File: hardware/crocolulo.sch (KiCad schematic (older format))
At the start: 8 parts, among them P1 CONN_02X14, P2 CONN_01X04, U1 stk682

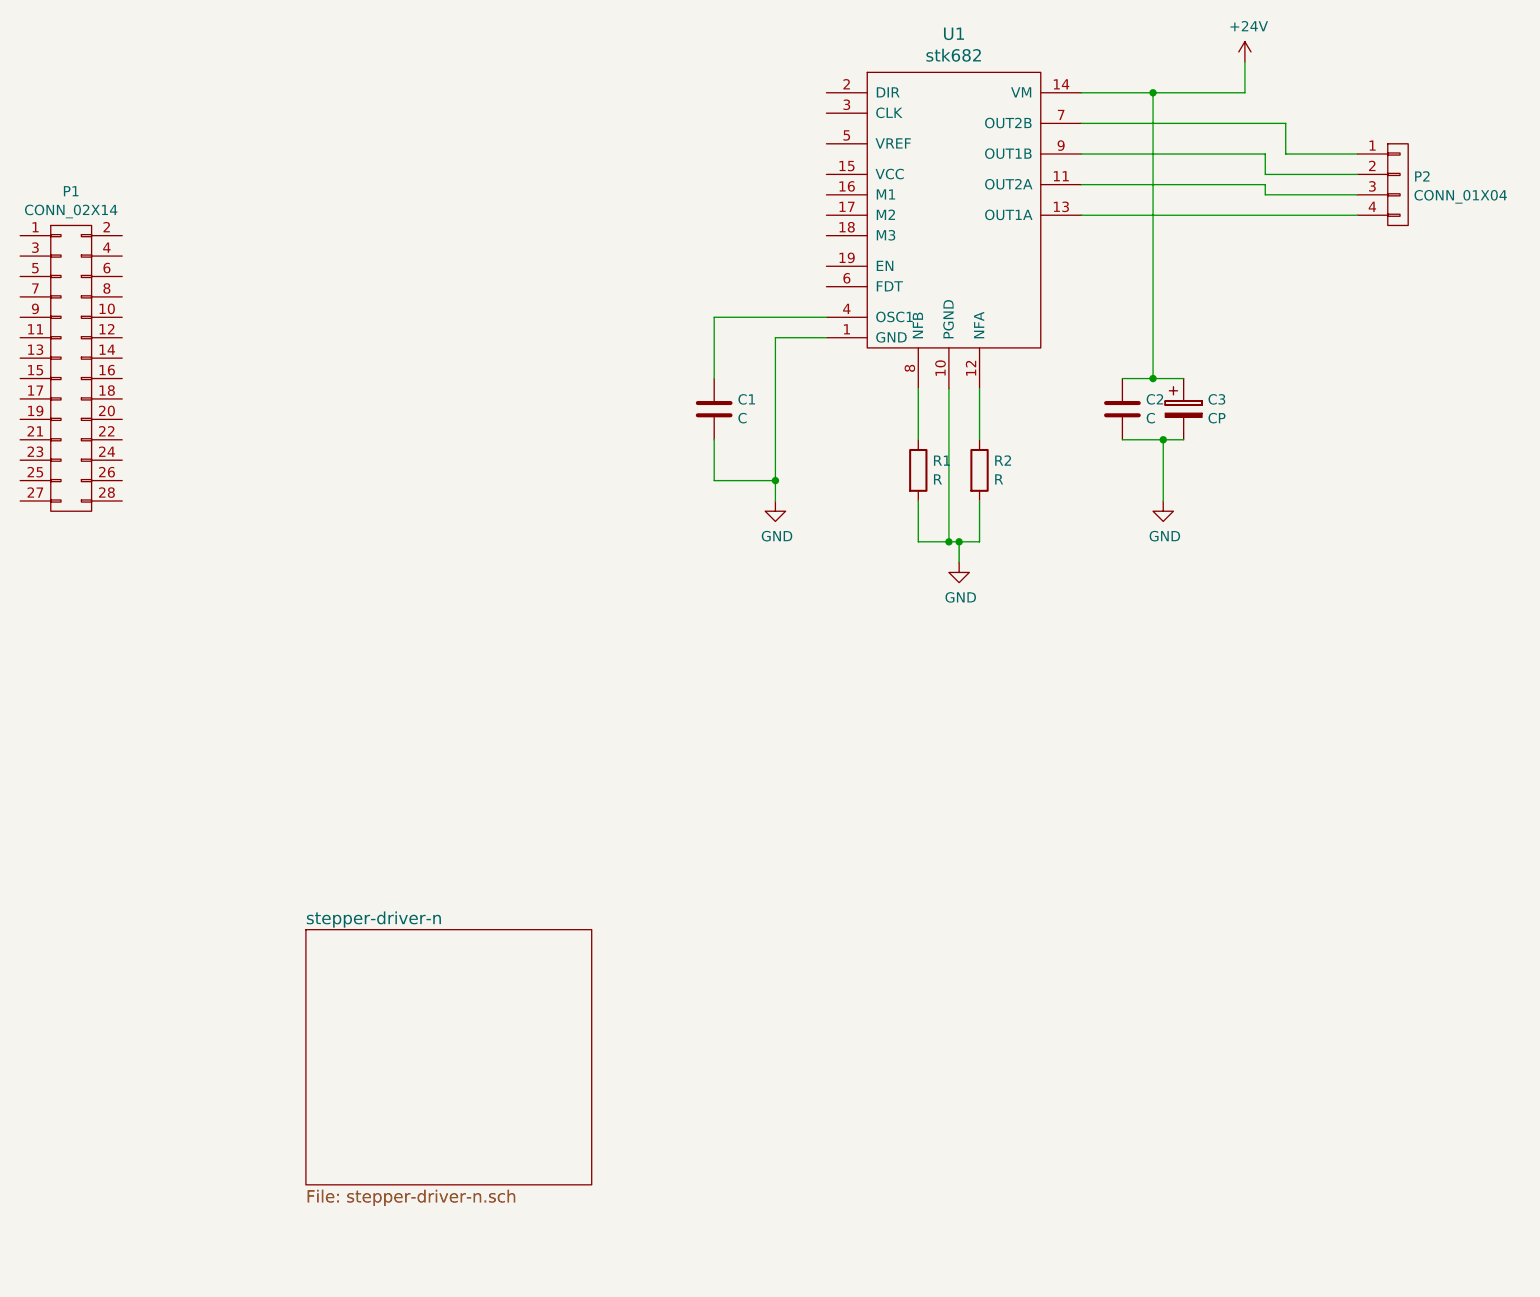
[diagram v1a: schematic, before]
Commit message: Add more sub sheets
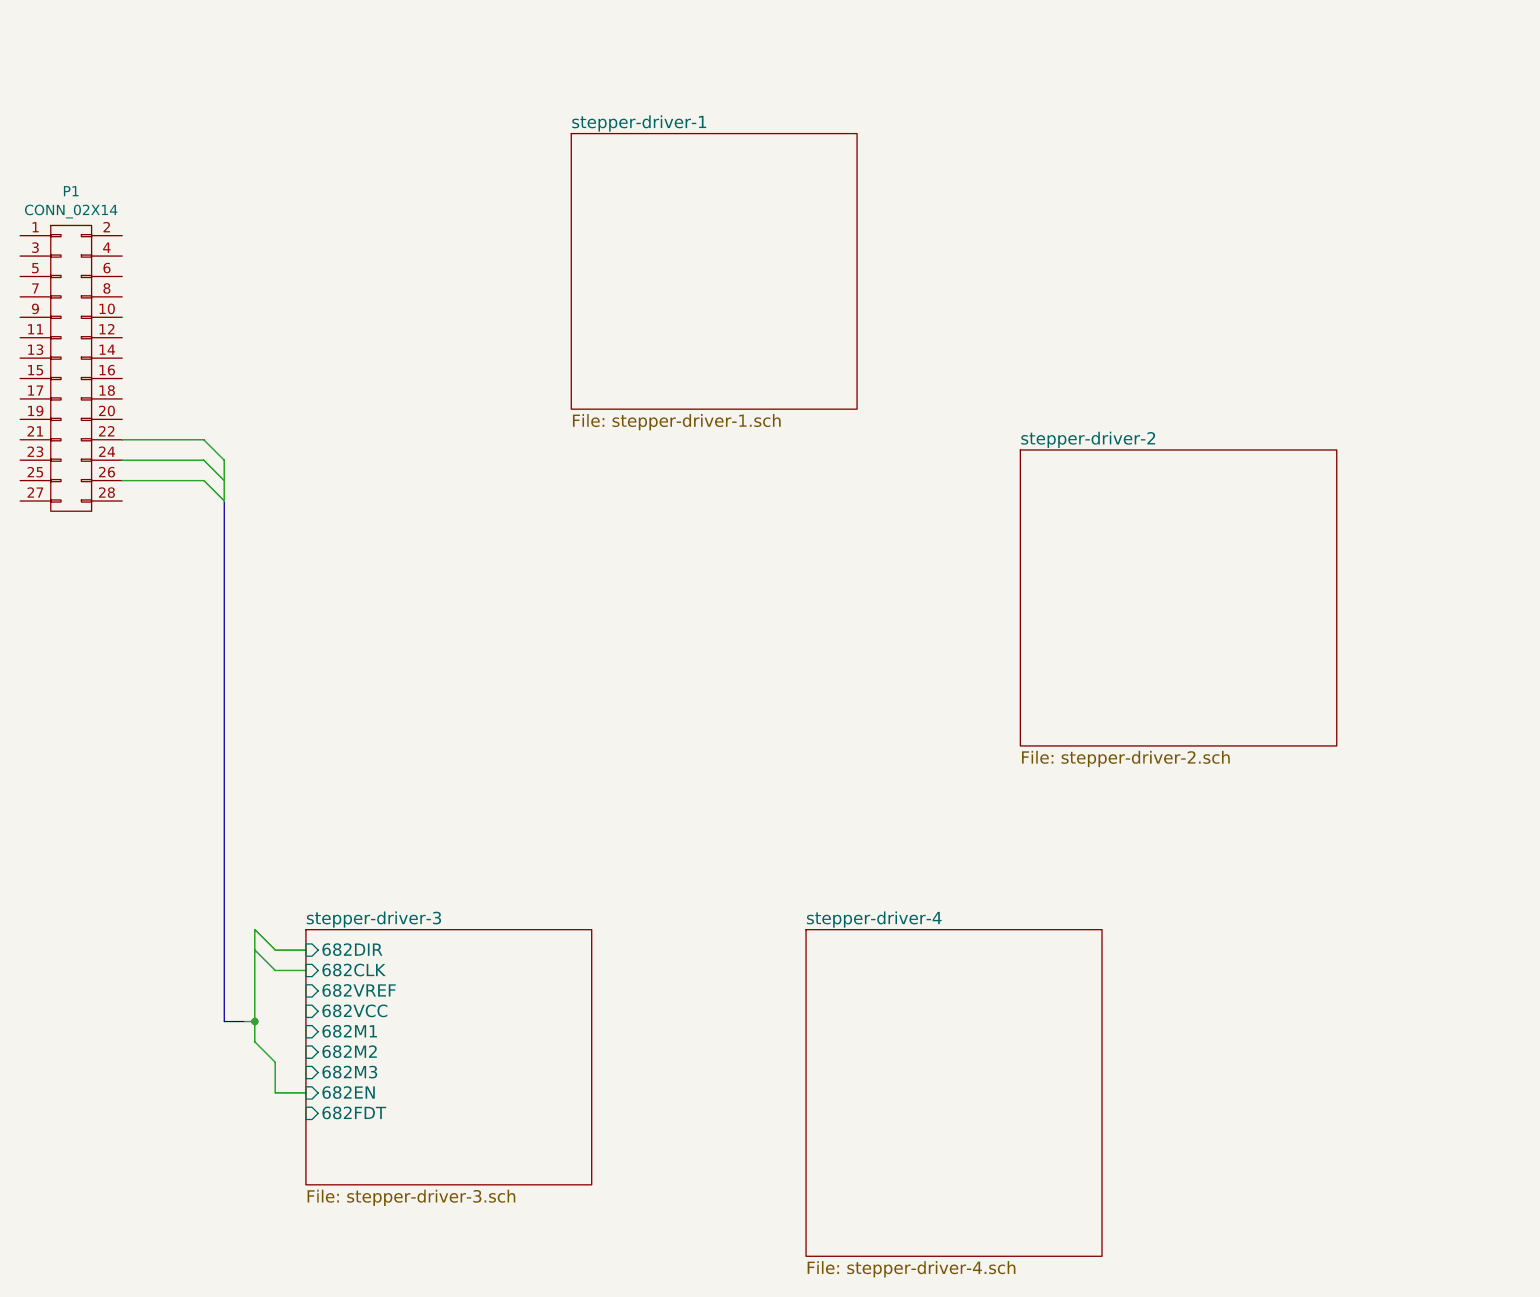
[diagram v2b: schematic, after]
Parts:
- removed C1, C2: C, symbol C
- removed C3: CP, symbol CP
- removed P2: CONN_01X04, symbol CONN_01X04
- removed R1, R2: R, symbol R
- removed U1: stk682, symbol stk682
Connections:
- net labels removed: +24V, GND
- wire segments 29 -> 13
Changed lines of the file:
@@
 $Descr A4 11693 8268
 encoding utf-8
-Sheet 1 2
+Sheet 1 4
 Title "Crocolulo Stepper Driver"
 Date ""
@@
 Comment4 ""
 $EndDescr
-$Comp
-L stk682 U1
-U 1 1 56C73EAB
-P 5850 1800
-F 0 "U1" H 5875 2587 60  0000 C CNN
-F 1 "stk682" H 5875 2481 60  0000 C CNN
-F 2 "" H 5850 1800 60  0000 C CNN
-F 3 "" H 5850 1800 60  0000 C CNN
-	1    5850 1800
-	1    0    0    -1
-$EndComp
-$Comp
-L C C1
-U 1 1 56C84AD0
-P 4700 2850
-F 0 "C1" H 4815 2896 50  0000 L CNN
-F 1 "C" H 4815 2804 50  0000 L CNN
-F 2 "" H 4738 2700 50  0000 C CNN
-F 3 "" H 4700 2850 50  0000 C CNN
-	1    4700 2850
-	1    0    0    -1
-$EndComp
-Wire Wire Line
-	4700 2700 4700 2400
-Wire Wire Line
-	4700 2400 5250 2400
-$Comp
-L GND #PWR1
-U 1 1 56C84B13
-P 5000 3300
-F 0 "#PWR1" H 5000 3050 50  0001 C CNN
-F 1 "GND" H 5008 3126 50  0000 C CNN
-F 2 "" H 5000 3300 50  0000 C CNN
-F 3 "" H 5000 3300 50  0000 C CNN
-	1    5000 3300
-	1    0    0    -1
-$EndComp
-Wire Wire Line
-	5000 3300 5000 2500
-Wire Wire Line
-	5000 2500 5250 2500
-Wire Wire Line
-	4700 3000 4700 3200
-Wire Wire Line
-	4700 3200 5000 3200
-Connection ~ 5000 3200
-$Comp
-L R R1
-U 1 1 56C84B3E
-P 5700 3150
-F 0 "R1" H 5770 3196 50  0000 L CNN
-F 1 "R" H 5770 3104 50  0000 L CNN
-F 2 "" V 5630 3150 50  0000 C CNN
-F 3 "" H 5700 3150 50  0000 C CNN
-	1    5700 3150
-	1    0    0    -1
-$EndComp
-$Comp
-L R R2
-U 1 1 56C84B76
-P 6000 3150
-F 0 "R2" H 6070 3196 50  0000 L CNN
-F 1 "R" H 6070 3104 50  0000 L CNN
-F 2 "" V 5930 3150 50  0000 C CNN
-F 3 "" H 6000 3150 50  0000 C CNN
-	1    6000 3150
-	1    0    0    -1
-$EndComp
-$Comp
-L GND #PWR2
-U 1 1 56C84B9A
-P 5900 3600
-F 0 "#PWR2" H 5900 3350 50  0001 C CNN
-F 1 "GND" H 5908 3426 50  0000 C CNN
-F 2 "" H 5900 3600 50  0000 C CNN
-F 3 "" H 5900 3600 50  0000 C CNN
-	1    5900 3600
-	1    0    0    -1
-$EndComp
-Wire Wire Line
-	6000 2750 6000 3000
-Wire Wire Line
-	5700 2750 5700 3000
-Wire Wire Line
-	5850 2750 5850 3500
-Wire Wire Line
-	5700 3500 6000 3500
-Wire Wire Line
-	5900 3500 5900 3600
-Wire Wire Line
-	5700 3300 5700 3500
-Connection ~ 5850 3500
-Wire Wire Line
-	6000 3500 6000 3300
-Connection ~ 5900 3500
-$Comp
-L CONN_01X04 P2
-U 1 1 56C84C17
-P 8050 1750
-F 0 "P2" H 8127 1788 50  0000 L CNN
-F 1 "CONN_01X04" H 8127 1696 50  0000 L CNN
-F 2 "" H 8050 1750 50  0000 C CNN
-F 3 "" H 8050 1750 50  0000 C CNN
-	1    8050 1750
-	1    0    0    -1
-$EndComp
-$Comp
-L +24V #PWR4
-U 1 1 56C84C67
-P 7300 1150
-F 0 "#PWR4" H 7300 1000 50  0001 C CNN
-F 1 "+24V" H 7318 1324 50  0000 C CNN
-F 2 "" H 7300 1150 50  0000 C CNN
-F 3 "" H 7300 1150 50  0000 C CNN
-	1    7300 1150
-	1    0    0    -1
-$EndComp
-Wire Wire Line
-	6500 1300 7300 1300
-Wire Wire Line
-	7300 1300 7300 1150
-Wire Wire Line
-	6500 1450 7500 1450
-Wire Wire Line
-	7500 1450 7500 1600
-Wire Wire Line
-	7500 1600 7850 1600
-Wire Wire Line
-	6500 1600 7400 1600
-Wire Wire Line
-	7400 1600 7400 1700
-Wire Wire Line
-	7400 1700 7850 1700
-Wire Wire Line
-	6500 1750 7400 1750
-Wire Wire Line
-	7400 1750 7400 1800
-Wire Wire Line
-	7400 1800 7850 1800
-Wire Wire Line
-	6500 1900 7850 1900
-$Comp
-L C C2
-U 1 1 56C84F28
-P 6700 2850
-F 0 "C2" H 6815 2896 50  0000 L CNN
-F 1 "C" H 6815 2804 50  0000 L CNN
-F 2 "" H 6738 2700 50  0000 C CNN
-F 3 "" H 6700 2850 50  0000 C CNN
-	1    6700 2850
-	1    0    0    -1
-$EndComp
-$Comp
-L CP C3
-U 1 1 56C84F62
-P 7000 2850
-F 0 "C3" H 7118 2896 50  0000 L CNN
-F 1 "CP" H 7118 2804 50  0000 L CNN
-F 2 "" H 7038 2700 50  0000 C CNN
-F 3 "" H 7000 2850 50  0000 C CNN
-	1    7000 2850
-	1    0    0    -1
-$EndComp
-Wire Wire Line
-	6700 2700 7000 2700
-Wire Wire Line
-	6850 2700 6850 1300
-Connection ~ 6850 1300
-Connection ~ 6850 2700
-Wire Wire Line
-	6700 3000 7000 3000
-$Comp
-L GND #PWR3
-U 1 1 56C85015
-P 6900 3300
-F 0 "#PWR3" H 6900 3050 50  0001 C CNN
-F 1 "GND" H 6908 3126 50  0000 C CNN
-F 2 "" H 6900 3300 50  0000 C CNN
-F 3 "" H 6900 3300 50  0000 C CNN
-	1    6900 3300
-	1    0    0    -1
-$EndComp
-Wire Wire Line
-	6900 3300 6900 3000
-Connection ~ 6900 3000
 $Comp
 L CONN_02X14 P1
@@
 S 2700 5400 1400 1250
 U 56C9E55A
-F0 "stepper-driver-n" 60
-F1 "stepper-driver-n.sch" 60
+F0 "stepper-driver-3" 60
+F1 "stepper-driver-3.sch" 60
+F2 "682DIR" I L 2700 5500 60
+F3 "682CLK" I L 2700 5600 60
+F4 "682VREF" I L 2700 5700 60
+F5 "682VCC" I L 2700 5800 60
+F6 "682M1" I L 2700 5900 60
+F7 "682M2" I L 2700 6000 60
+F8 "682M3" I L 2700 6100 60
+F9 "682EN" I L 2700 6200 60
+F10 "682FDT" I L 2700 6300 60
+$EndSheet
+Entry Wire Line
+	2200 3200 2300 3300
+Wire Bus Line
+	2300 3300 2300 5850
+Wire Bus Line
+	2300 5850 2400 5850
+Wire Wire Line
+	1800 3200 2200 3200
+Entry Wire Line
+	2200 3100 2300 3200
+Entry Wire Line
+	2200 3000 2300 3100
+Wire Wire Line
+	1800 3100 2200 3100
+Wire Wire Line
+	2200 3000 1800 3000
+Wire Wire Line
+	2300 3100 2300 3200
+Wire Wire Line
+	2300 3200 2300 3300
+Entry Wire Line
+	2450 5950 2550 6050
+Entry Wire Line
+	2450 5400 2550 5500
+Entry Wire Line
+	2450 5500 2550 5600
+Wire Wire Line
+	2400 5850 2450 5850
+Wire Wire Line
+	2450 5400 2450 5500
+Wire Wire Line
+	2450 5500 2450 5850
+Wire Wire Line
+	2450 5850 2450 5950
+Connection ~ 2450 5850
+Wire Wire Line
+	2550 5500 2700 5500
+Wire Wire Line
+	2550 5600 2700 5600
+Wire Wire Line
+	2550 6050 2550 6200
+Wire Wire Line
+	2550 6200 2700 6200
+$Sheet
+S 4000 1500 1400 1350
+U 56CA076F
+F0 "stepper-driver-1" 60
+F1 "stepper-driver-1.sch" 60
+$EndSheet
+$Sheet
+S 6200 3050 1550 1450
+U 56CA07F7
+F0 "stepper-driver-2" 60
+F1 "stepper-driver-2.sch" 60
+$EndSheet
+$Sheet
+S 5150 5400 1450 1600
+U 56CA087F
+F0 "stepper-driver-4" 60
+F1 "stepper-driver-4.sch" 60
 $EndSheet
 $EndSCHEMATC
